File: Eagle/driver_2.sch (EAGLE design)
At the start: 21 parts, among them CON1 V6, CON4 V2, CON5 V1, CON6 VA, CON7 VB, CON8 V3, IC1 74HC688N, IC4 74HC688N, IC5 74HC32N

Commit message: Added files via upload
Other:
- note added: "Address Bus"
- note added: "Hold on address"
- note removed: "Adress Bus"
- note removed: "Hold on adress"
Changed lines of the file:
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@@
 <sheet>
 <plain>
-<text x="109.22" y="167.64" size="6.4516" layer="91">Adress Bus</text>
+<text x="109.22" y="167.64" size="6.4516" layer="91">Address Bus</text>
 <text x="127" y="154.94" size="3.81" layer="91">Low</text>
 <text x="127" y="91.44" size="3.81" layer="91">High</text>
 <text x="256.54" y="152.4" size="3.81" layer="91">Low</text>
 <text x="259.08" y="81.28" size="3.81" layer="91">High</text>
-<text x="231.14" y="167.64" size="6.4516" layer="91">Hold on adress</text>
+<text x="231.14" y="167.64" size="6.4516" layer="91">Hold on address</text>
 <text x="317.5" y="88.9" size="1.778" layer="91">To A29 on Backplane bus or IC32 pin 13 on the Clock-Control Board</text>
 </plain>

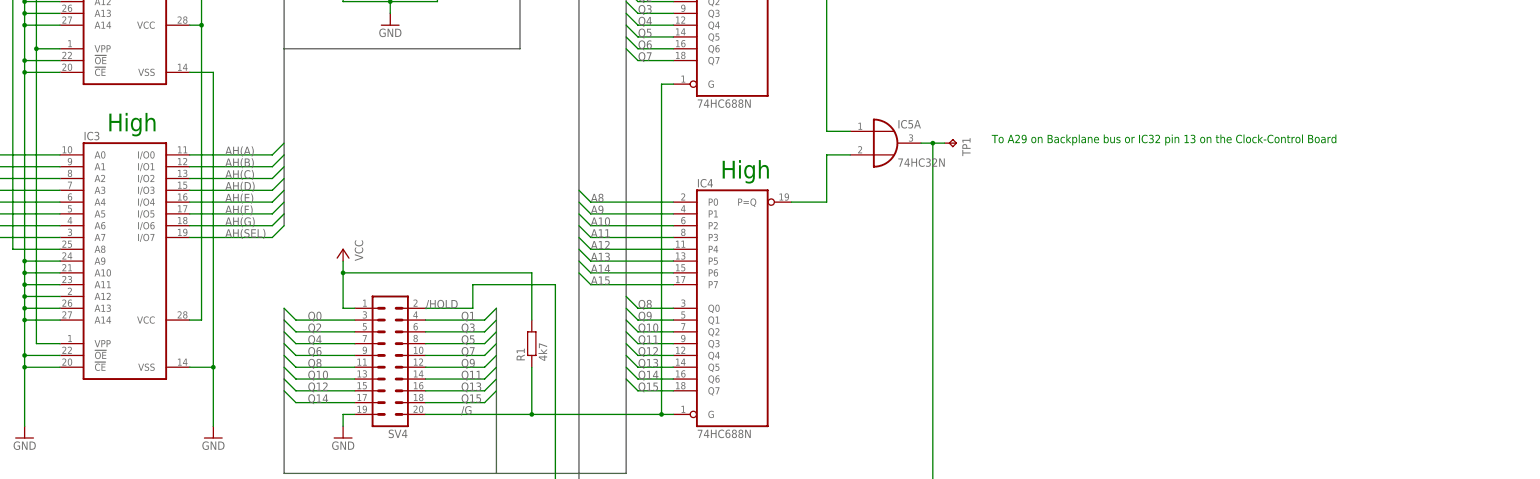
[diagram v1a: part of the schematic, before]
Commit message: Bug fix
Fogrot to add a diode to /HALT Signal... very bad :-(
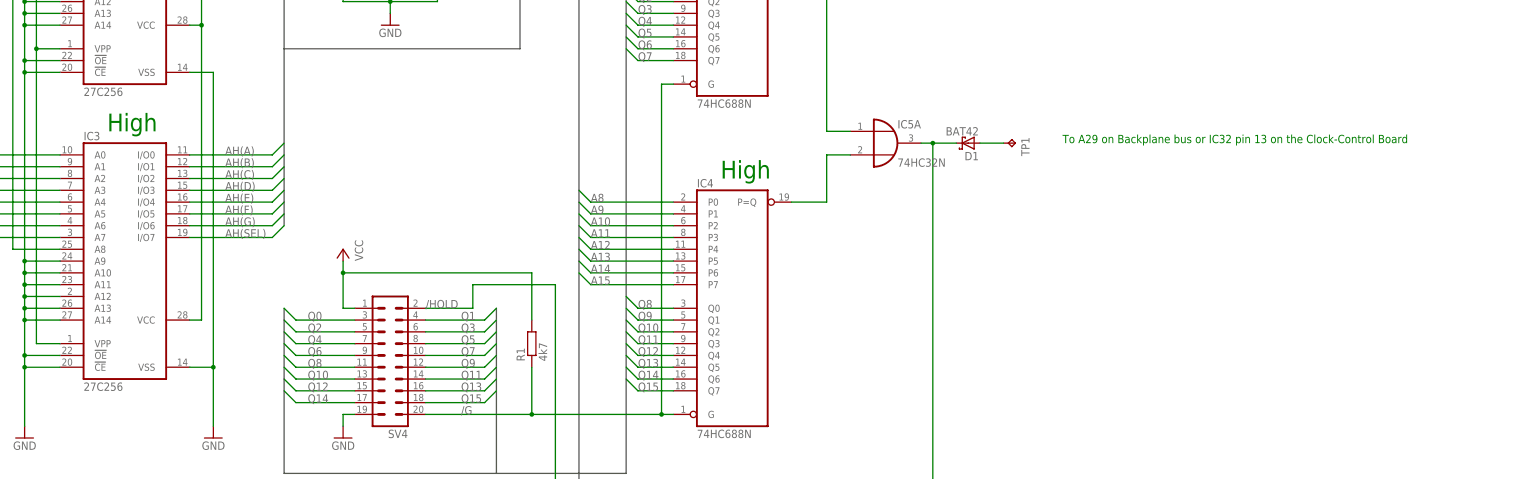
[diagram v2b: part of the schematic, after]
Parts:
- added D1: BAT42, diode:BAT42
- IC2, IC3: value (none) -> 27C256
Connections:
- new net N$5: D1.A, TP1.TP
- net /HOLD: now also D1.C; no longer TP1.TP
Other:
- moved on the sheet: TP1
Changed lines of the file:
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@@
 <layer number="97" name="Info" color="7" fill="1" visible="yes" active="yes"/>
 <layer number="98" name="Guide" color="6" fill="1" visible="yes" active="yes"/>
+<layer number="99" name="SpiceOrder" color="5" fill="1" visible="yes" active="yes"/>
 </layers>
 <schematic xreflabel="%F%N/%S.%C%R" xrefpart="/%S.%C%R">
@@
 <part name="CON7" library="con-ml" deviceset="ML10" device="" value="VB"/>
 <part name="CON8" library="con-ml" deviceset="ML14" device="" value="V3"/>
-<part name="IC2" library="memory-hitachi" deviceset="27C256AG" device=""/>
-<part name="IC3" library="memory-hitachi" deviceset="27C256AG" device=""/>
+<part name="IC2" library="memory-hitachi" deviceset="27C256AG" device="" value="27C256"/>
+<part name="IC3" library="memory-hitachi" deviceset="27C256AG" device="" value="27C256"/>
 <part name="P+1" library="supply1" deviceset="VCC" device=""/>
 <part name="P+5" library="supply1" deviceset="VCC" device=""/>
@@
 <part name="P+3" library="supply1" deviceset="VCC" device=""/>
 <part name="R1" library="rcl" deviceset="R-EU_" device="0204/5" value="4k7"/>
+<part name="D1" library="diode" deviceset="BAT42" device=""/>
 </parts>
 <sheets>
@@
 <text x="259.08" y="81.28" size="3.81" layer="91">High</text>
 <text x="231.14" y="167.64" size="6.4516" layer="91">Hold on address</text>
-<text x="317.5" y="88.9" size="1.778" layer="91">To A29 on Backplane bus or IC32 pin 13 on the Clock-Control Board</text>
+<text x="332.74" y="88.9" size="1.778" layer="91">To A29 on Backplane bus or IC32 pin 13 on the Clock-Control Board</text>
 </plain>
 <instances>
@@
 <instance part="C4" gate="G$1" x="83.82" y="30.48"/>
 <instance part="IC5" gate="A" x="294.64" y="88.9"/>
-<instance part="TP1" gate="G$1" x="309.88" y="88.9" rot="R270"/>
+<instance part="TP1" gate="G$1" x="322.58" y="88.9" rot="R270"/>
 <instance part="GND1" gate="1" x="177.8" y="25.4" rot="MR0"/>
 <instance part="SV4" gate="1" x="187.96" y="40.64" rot="R180"/>
 <instance part="P+3" gate="VCC" x="177.8" y="66.04" rot="MR0"/>
 <instance part="R1" gate="G$1" x="218.44" y="45.72" rot="R90"/>
+<instance part="D1" gate="1" x="312.42" y="88.9" rot="R180"/>
 </instances>
 <busses>
@@
 <wire x1="223.52" y1="58.42" x2="223.52" y2="7.62" width="0.1524" layer="91"/>
 <pinref part="IC5" gate="A" pin="O"/>
-<pinref part="TP1" gate="G$1" pin="TP"/>
 <wire x1="302.26" y1="88.9" x2="304.8" y2="88.9" width="0.1524" layer="91"/>
-<wire x1="304.8" y1="88.9" x2="307.34" y2="88.9" width="0.1524" layer="91"/>
 <wire x1="223.52" y1="7.62" x2="304.8" y2="7.62" width="0.1524" layer="91"/>
 <wire x1="304.8" y1="7.62" x2="304.8" y2="88.9" width="0.1524" layer="91"/>
+<label x="195.58" y="53.34" size="1.778" layer="95"/>
+<pinref part="D1" gate="1" pin="C"/>
+<wire x1="309.88" y1="88.9" x2="304.8" y2="88.9" width="0.1524" layer="91"/>
 <junction x="304.8" y="88.9"/>
-<label x="195.58" y="53.34" size="1.778" layer="95"/>
-</segment>
-</net>
+</segment>
+</net>
+<net name="N$5" class="0">
+<segment>
+<pinref part="D1" gate="1" pin="A"/>
+<pinref part="TP1" gate="G$1" pin="TP"/>
+<wire x1="314.96" y1="88.9" x2="320.04" y2="88.9" width="0.1524" layer="91"/>
+</segment>
+</net>
